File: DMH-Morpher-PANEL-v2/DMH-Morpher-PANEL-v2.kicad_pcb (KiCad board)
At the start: 2 copper layers, 100 x 200 mm, 50 parts, among them J0 Panel_GND_Solder_Wire_Pad

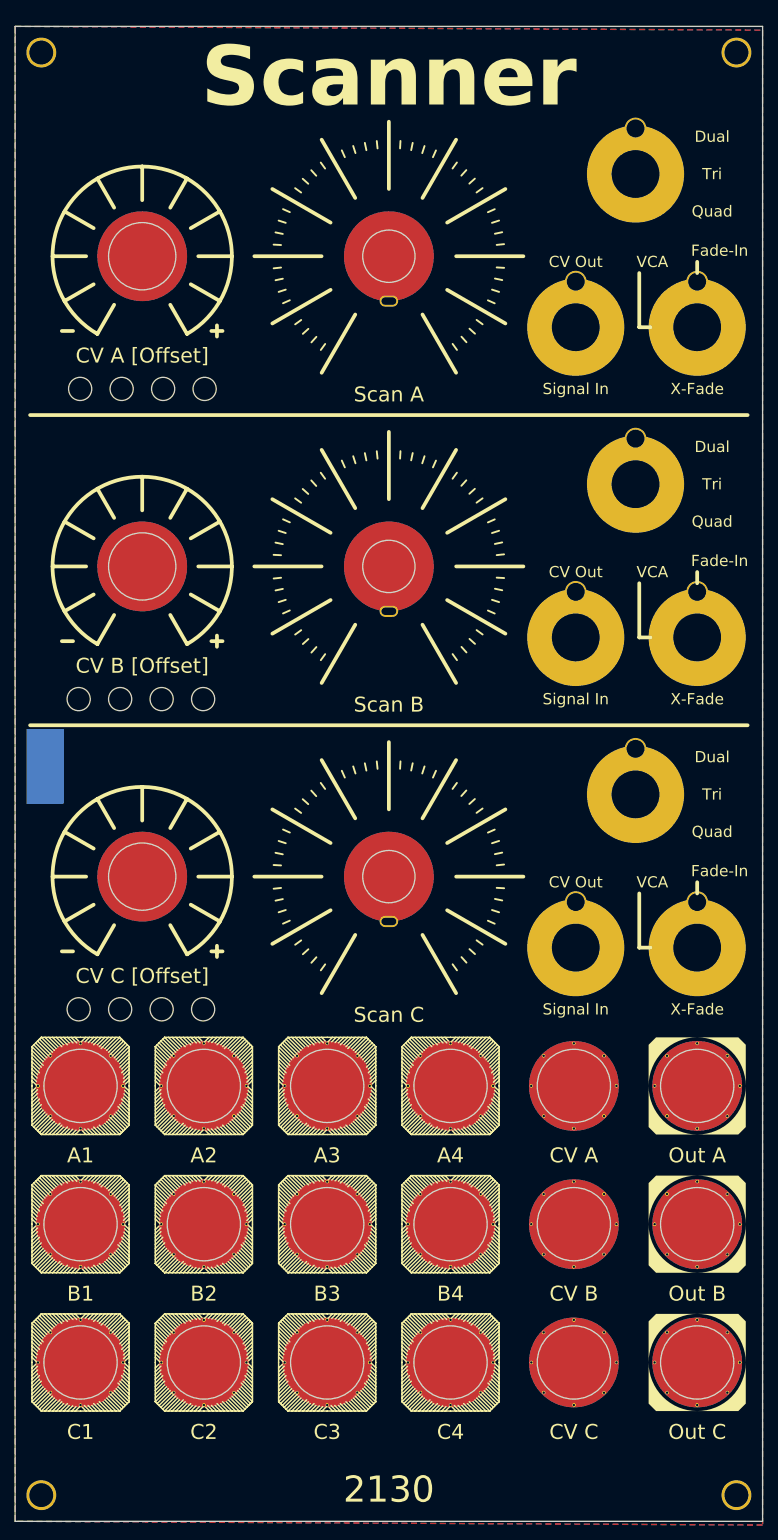
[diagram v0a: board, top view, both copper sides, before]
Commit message: KiCad 10
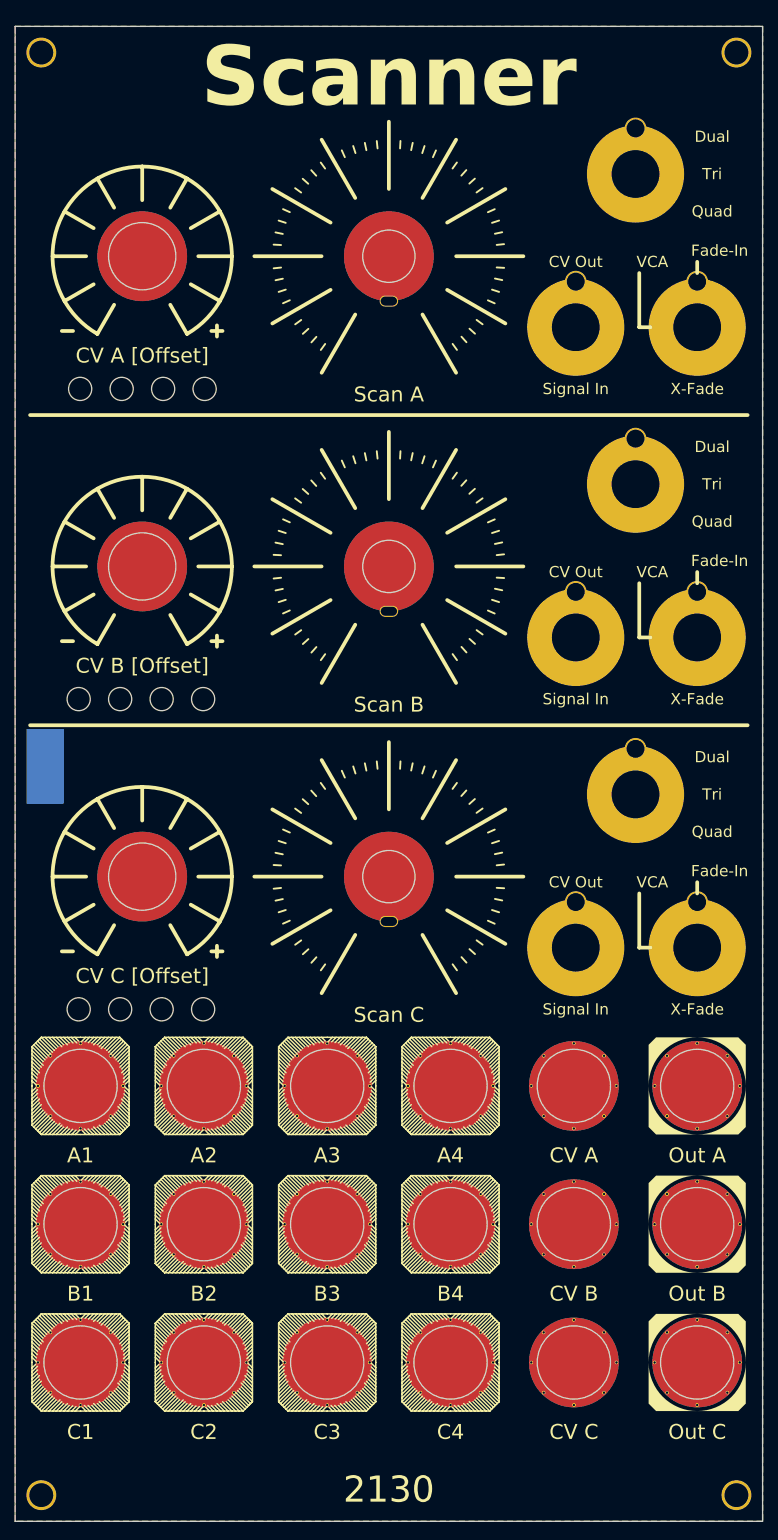
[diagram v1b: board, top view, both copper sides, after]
